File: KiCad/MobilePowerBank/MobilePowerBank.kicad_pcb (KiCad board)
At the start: 2 copper layers, 114 x 164 mm, 185 parts, among them J1 Power IN, J2 Power OUT 2, J3 Power OUT 1, J4 OLED I2C, J5 PDI, J6 OLED, J7 Power OUT 3, J8 Power OUT 4, J9 Power OUT 5, SW1 SW_DIP_x01, U1 INA169, U10 INA138, U11 LMZ14201H, U12 LMZ14201H, U13 INA138, U14 INA138, U15 ATXMEGA256A3U-AU, U2 LMZ14203H, U3 L78M12, U4 INA138, U5 UA78M33, U7 LMZ14203H, U8 LMZ14203H, U9 INA138

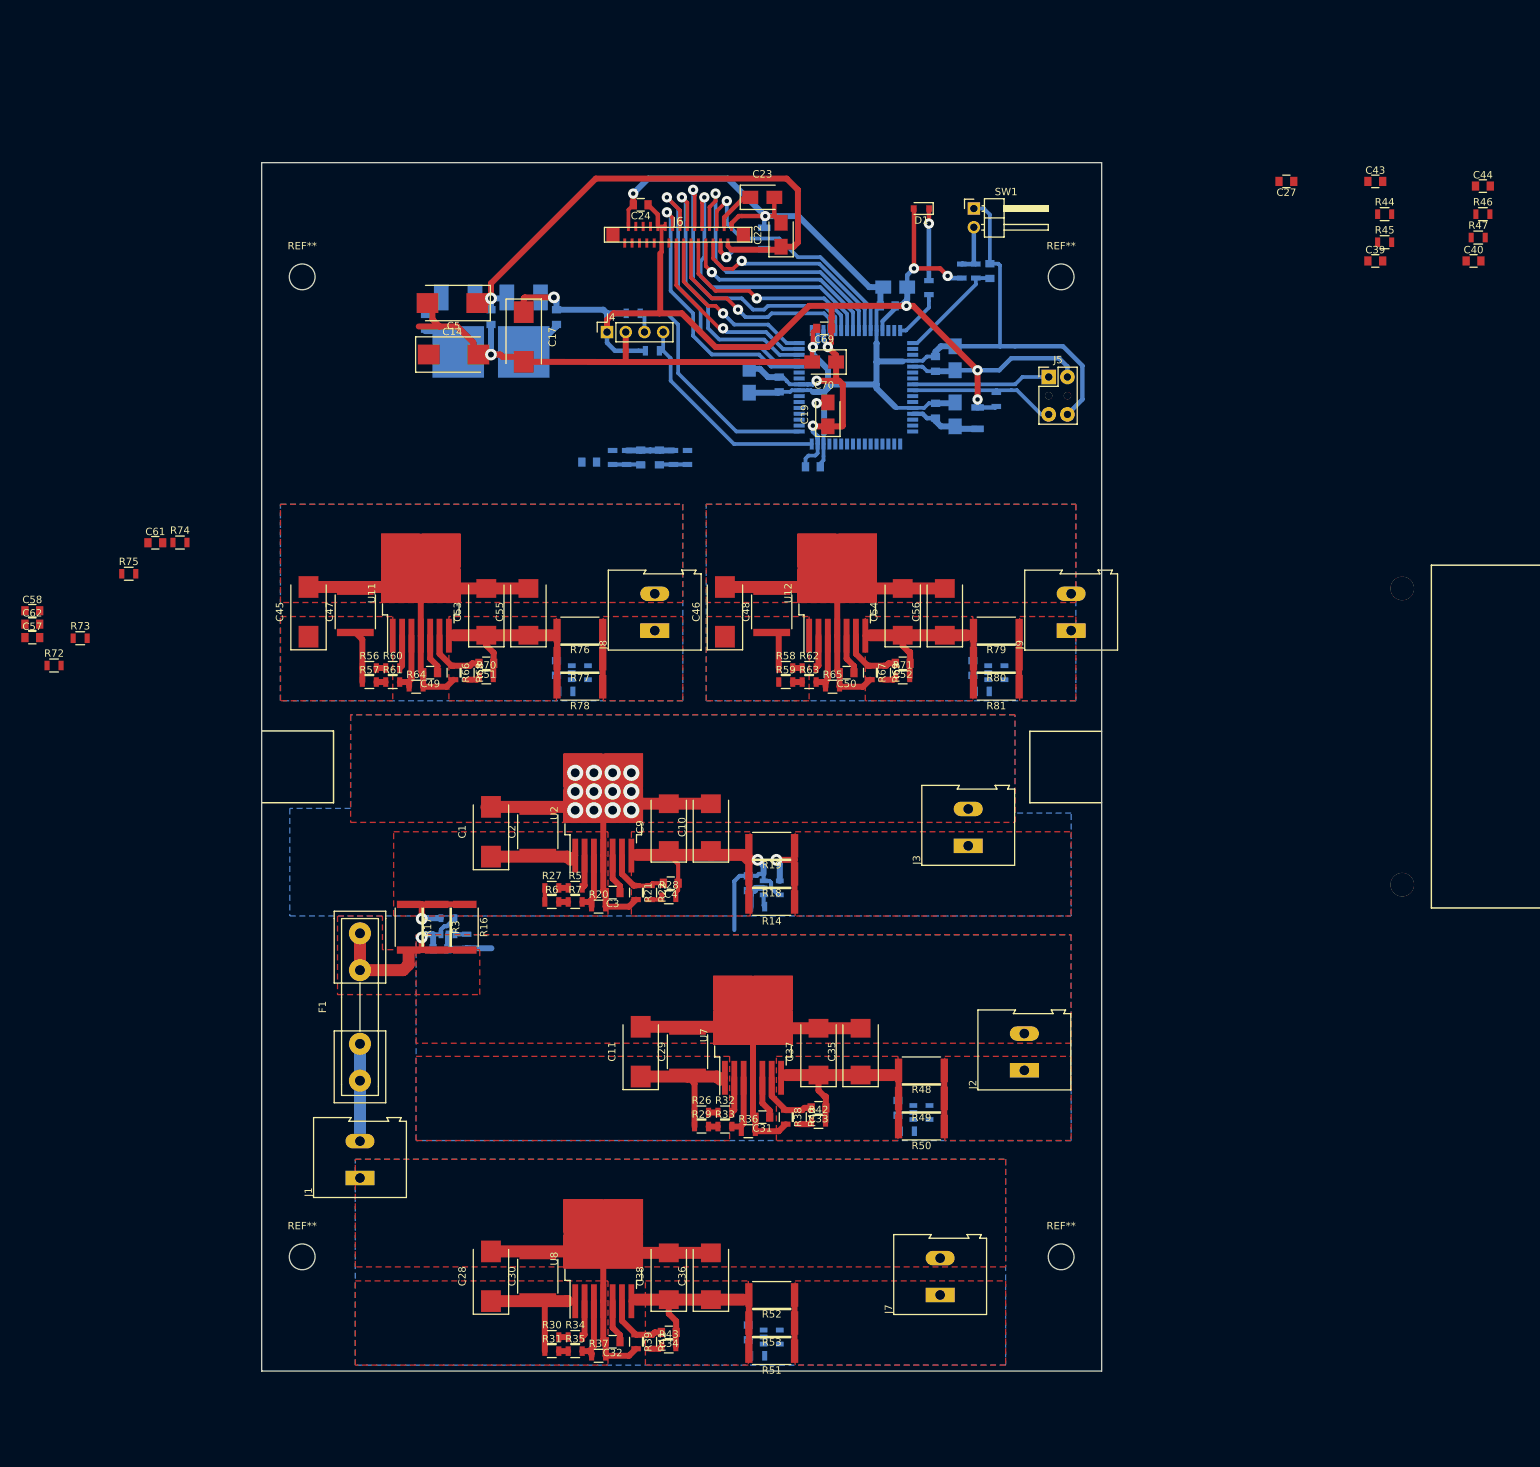
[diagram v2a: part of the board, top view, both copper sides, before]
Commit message: Bigger case
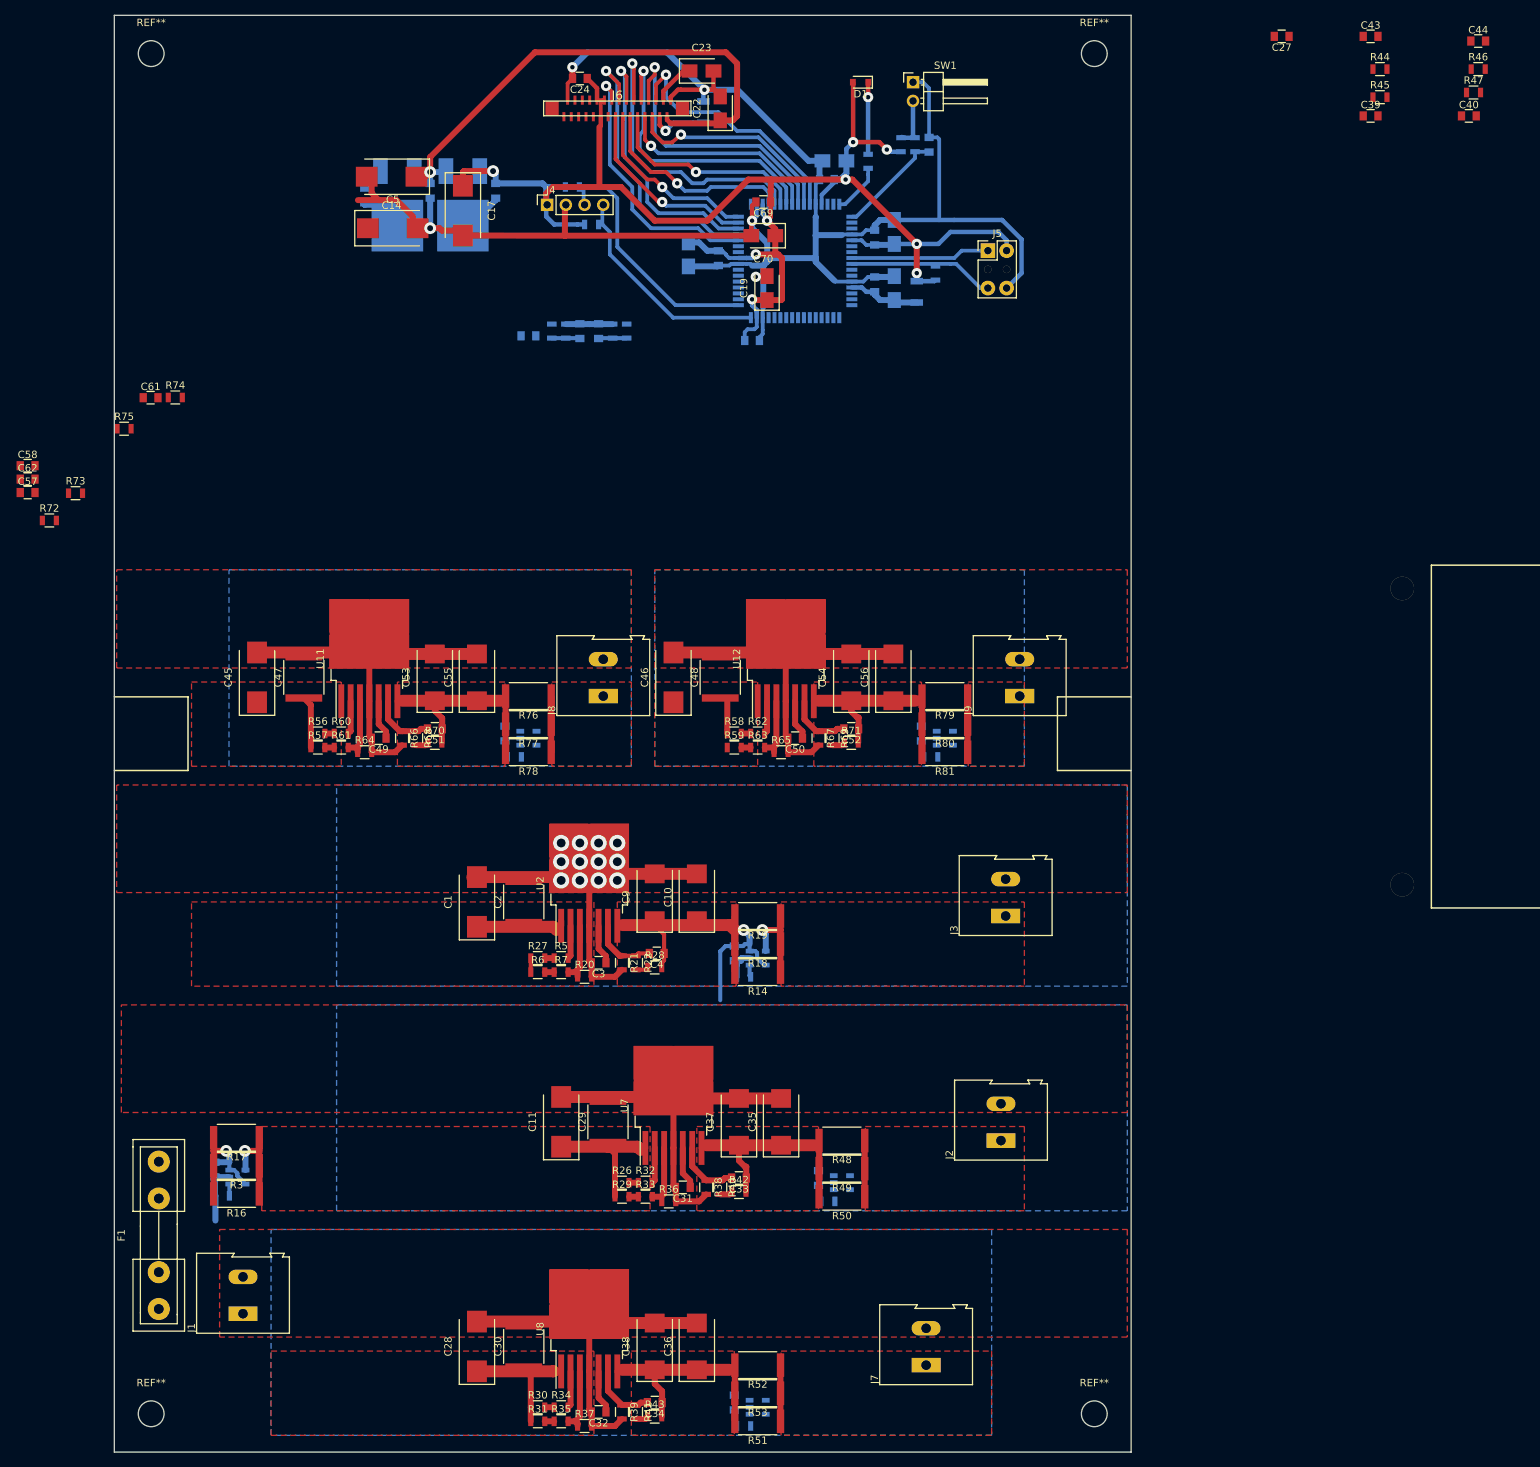
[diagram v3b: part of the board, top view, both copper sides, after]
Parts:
- moved R4 47.9 mm to (34.7, 180.2), turned to 180 degrees
- moved R16 47.6 mm to (36.6, 180.0), turned to 180 degrees
- moved U1 44.4 mm to (36.7, 177.7), turned to 0 degrees
- moved C7 42.8 mm to (33.7, 176.7), turned to 90 degrees
- moved R3 42.3 mm to (36.6, 176.1), turned to 180 degrees
- moved F1 41.3 mm to (26.0, 195.6)
- moved R17 36.9 mm to (36.6, 172.3), turned to 180 degrees
- moved REF** 36.6 mm to (25.0, 25.2)
- moved REF** 30.6 mm to (153.0, 25.2)
- moved REF** 29.6 mm to (25.0, 209.8)
- moved J1 24.3 mm to (37.5, 196.2)
- moved REF** 21.8 mm to (153.0, 209.8)
- moved R46 19.7 mm to (205.1, 27.3)
- moved C44 19.7 mm to (205.1, 23.5)
- moved C27 19.7 mm to (178.4, 22.9)
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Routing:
- net VDD: track 31.3 -> 17.5 mm
- net Net-(F1-Pad1): track 13.2 -> 0.00 mm
- removed copper zone on F.Cu, net VDD
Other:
- board size 114 x 164 mm -> 138 x 195 mm

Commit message: PCB major work
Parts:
- added C71: 47u, Capacitors_Tantalum_SMD:CP_Tantalum_Case-V_EIA-7343-20_Wave, F.Cu at (36.2, 78.7)
- added C72: 10u/35V/X7R, Capacitors_SMD:C_2220, F.Cu at (42.5, 78.7)
- added C73: 4u7, Capacitors_SMD:C_0805, F.Cu at (52.7, 87.0)
- added C74: 22n, Capacitors_SMD:C_0805, F.Cu at (60.3, 85.7)
- added C75: 47u/1-45mESR, Capacitors_Tantalum_SMD:CP_Tantalum_Case-D_EIA-7343-31_Reflow, F.Cu at (60.3, 78.7)
- added C76: 47u/1-45mESR, Capacitors_Tantalum_SMD:CP_Tantalum_Case-D_EIA-7343-31_Reflow, F.Cu at (66.0, 78.7)
- added C77: 100n, Capacitors_SMD:C_0805, B.Cu at (107.3, 75.6)
- added C78: 100n, Capacitors_SMD:C_0805, B.Cu at (81.9, 86.4)
- added C79: 1u, Capacitors_SMD:C_0805, B.Cu at (108.6, 71.8)
- added J10: Power OUT 6, Connectors_Terminal_Blocks:TerminalBlock_Altech_AK300-2_P5.00mm, F.Cu at (96.5, 81.3)
- added R84: 220k, Resistors_SMD:R_0805, F.Cu at (44.5, 86.4)
- added R85: 30k, Resistors_SMD:R_0805, F.Cu at (44.5, 88.3)
- added R86: 30k, Resistors_SMD:R_0805, F.Cu at (47.6, 86.4)
- added R87: 300k, Resistors_SMD:R_0805, F.Cu at (47.6, 88.3)
- added R88: 20k, Resistors_SMD:R_0805, F.Cu at (50.8, 88.9)
- added R89: 2k2, Resistors_SMD:R_0805, F.Cu at (55.9, 87.0)
- added R90: 15k4, Resistors_SMD:R_0805, F.Cu at (57.8, 87.0)
- added R91: 15k4, Resistors_SMD:R_0805, F.Cu at (60.3, 87.6)
- added R92: 90k, Resistors_SMD:R_0805, B.Cu at (107.3, 77.5)
- added R93: 10k, Resistors_SMD:R_0805, B.Cu at (107.3, 73.7)
- added R94: 0R1, Resistors_SMD:R_2512, F.Cu at (85.1, 85.0)
- added R95: 0R1, Resistors_SMD:R_2512, F.Cu at (85.1, 88.8)
- added R96: 0R1, Resistors_SMD:R_2512, F.Cu at (85.1, 81.2)
- added R97: 20k, Resistors_SMD:R_0805, B.Cu at (83.2, 89.5)
- added R98: 0, Resistors_SMD:R_0805, F.Cu at (104.1, 59.7)
- added U16: INA138, TO_SOT_Packages_SMD:SOT-23-5, B.Cu at (85.1, 87.0)
- added U6: LMZ14203H, TO_SOT_Packages_SMD:TO-263-7_TabPin4, F.Cu at (51.4, 76.2)
- added x1: jumper, JPJumpers:Jumper_30x1.5, F.Cu at (52.7, 192.4)
- added x2: jumper, JPJumpers:Jumper_30x1.5, F.Cu at (45.1, 161.9)
- added x3: jumper, JPJumpers:Jumper_30x1.5, F.Cu at (39.4, 134.0)
- added x4: jumper, JPJumpers:Jumper_30x1.5, F.Cu at (35.6, 103.5)
- added x5: jumper, JPJumpers:Jumper_45x1.5, F.Cu at (31.1, 65.4)
- C27, C39, C40, C43, C44, C57, C58, C61, C62, R44, R45, R46, R47, R72, R73, R74, R75: moved to B.Cu
- moved C62 113.8 mm to (121.9, 78.1), turned to 270 degrees
- moved C58 111.8 mm to (120.0, 79.4), turned to 90 degrees
- moved C57 103.9 mm to (111.8, 75.6)
- moved R72 101.2 mm to (111.8, 77.5), turned to 180 degrees
- moved R73 97.7 mm to (111.8, 73.7)
- moved R75 96.8 mm to (118.1, 79.4), turned to 90 degrees
- moved R74 94.7 mm to (122.6, 81.3), turned to 180 degrees
- moved C61 88.4 mm to (113.3, 71.8), turned to 180 degrees
- moved R47 85.6 mm to (125.7, 64.1), turned to 90 degrees
- moved C44 85.2 mm to (129.5, 62.9), turned to 270 degrees
- moved R46 84.3 mm to (130.2, 66.0), turned to 180 degrees
- moved C40 82.1 mm to (127.6, 64.1), turned to 90 degrees
- moved R45 78.4 mm to (123.2, 69.1), turned to 90 degrees
- moved C43 77.9 mm to (127.0, 67.9), turned to 270 degrees
- moved R44 77.7 mm to (127.6, 71.1), turned to 180 degrees
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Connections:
- C1 pad 1: POWER_IN -> POWER_IN_1
- C2 pad 1: POWER_IN -> POWER_IN_1
- C26 pad 2: GND -> GNDA
- C27 pad 2: GND -> GNDA
- C28 pad 1: POWER_IN -> POWER_IN_3
- C30 pad 1: POWER_IN -> POWER_IN_3
- C39 pad 2: GND -> GNDA
- C41 pad 1: GND -> GNDA
- C42 pad 1: GND -> GNDA
- C43 pad 2: GND -> GNDA
- C45 pad 1: POWER_IN -> POWER_IN_4
- C47 pad 1: POWER_IN -> POWER_IN_4
- C5 pad 1: POWER_IN -> Net-(C5-Pad1)
- C57 pad 2: GND -> GNDA
- C58 pad 2: GND -> GNDA
- C59 pad 1: GND -> GNDA
- C6 pad 1: POWER_IN -> Net-(C5-Pad1)
- C60 pad 1: GND -> GNDA
- C61 pad 2: GND -> GNDA
- C62 pad 2: GND -> GNDA
- C8 pad 1: GND -> GNDA
- R12 pad 1: Net-(C10-Pad1) -> POWER_1_OUT
- R13 pad 2: GND -> GNDA
- R15 pad 2: GND -> GNDA
- R27 pad 1: POWER_IN -> POWER_IN_1
- R30 pad 1: POWER_IN -> POWER_IN_3
- R31 pad 1: POWER_IN -> POWER_IN_3
- R44 pad 1: Net-(C33-Pad1) -> POWER_2_OUT
- R45 pad 2: GND -> GNDA
- R46 pad 1: Net-(C34-Pad1) -> POWER_3_OUT
- R47 pad 2: GND -> GNDA
- R54 pad 2: GND -> GNDA
- R55 pad 2: GND -> GNDA
- R56 pad 1: POWER_IN -> POWER_IN_4
- R57 pad 1: POWER_IN -> POWER_IN_4
- R6 pad 1: POWER_IN -> POWER_IN_1
- R72 pad 1: Net-(C51-Pad1) -> POWER_4_OUT
- R73 pad 2: GND -> GNDA
- R74 pad 1: Net-(C52-Pad1) -> POWER_5_OUT
- R75 pad 2: GND -> GNDA
- R82 pad 2: GND -> GNDA
- R83 pad 2: GND -> GNDA
- U10 pad 2: GND -> GNDA
- U11 pad 1: POWER_IN -> POWER_IN_4
- U13 pad 2: GND -> GNDA
- U14 pad 2: GND -> GNDA
- U15 pad 1: (no net) -> OUT_2_Current
- U15 pad 10: (no net) -> OUT_6_Voltage
- U15 pad 11: (no net) -> IN_Current
- U15 pad 12: (no net) -> IN_Voltage
- U15 pad 2: (no net) -> OUT_2_Voltage
- U15 pad 3: (no net) -> OUT_1_Current
- U15 pad 4: (no net) -> OUT_1_Voltage
- U15 pad 5: (no net) -> OUT_5_Current
- U15 pad 6: (no net) -> OUT_5_Voltage
- U15 pad 63: (no net) -> OUT_3_Current
- U15 pad 64: (no net) -> OUT_3_Voltage
- U15 pad 7: (no net) -> OUT_4_Current
- U15 pad 8: (no net) -> OUT_4_Voltage
- U15 pad 9: (no net) -> OUT_6_Current
- U2 pad 1: POWER_IN -> POWER_IN_1
- U3 pad 1: POWER_IN -> Net-(C5-Pad1)
- U4 pad 2: GND -> GNDA
- U8 pad 1: POWER_IN -> POWER_IN_3
- U9 pad 2: GND -> GNDA
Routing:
- net IN_Current: track 1.90 -> 232.2 mm
- net OUT_3_Current: track 0.00 -> 217.7 mm
- net VDD: track 17.5 -> 224.1 mm
- net OUT_2_Current: track 0.00 -> 179.0 mm
- net POWER_3_OUT: track 7.62 -> 183.7 mm, vias 0 -> 1
- net OUT_1_Current: track 1.65 -> 158.0 mm
- net POWER_2_OUT: track 7.62 -> 136.2 mm, vias 0 -> 1
- net GNDA: track 309.8 -> 436.9 mm, vias 12 -> 59
- net POWER_1_OUT: track 13.1 -> 104.5 mm
- net OUT_4_Current: track 0.00 -> 85.4 mm
- net OUT_5_Current: track 0.00 -> 58.9 mm
- net POWER_4_OUT: track 7.62 -> 59.7 mm, vias 0 -> 1
- net Net-(C74-Pad1): track 0.00 -> 50.9 mm, vias 0 -> 1
- net OUT_6_Current: track 0.00 -> 50.4 mm
- net POWER_IN_1: track 0.00 -> 46.6 mm
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- added copper zone on B.Cu, net GND
- added copper zone on F.Cu, net Net-(C74-Pad1)
- added copper zone on B.Cu, net Net-(F1-Pad1)
- added copper zone on F.Cu, net Net-(F1-Pad1)
- added copper zone on F.Cu, net POWER_6_OUT
- added copper zone on F.Cu, net POWER_IN_1
- added copper zone on F.Cu, net POWER_IN_3
- added copper zone on F.Cu, net POWER_IN_4
- added copper zone on F.Cu, net POWER_IN_6
- added copper zone on F.Cu, net VDD

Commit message: PCB finish, BOM check
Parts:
- added x6: jumper, JPJumpers:Jumper_30x1.5, F.Cu at (44.7, 146.7)
- added x7: jumper, JPJumpers:Jumper_30x1.5, F.Cu at (52.3, 177.2)
- added x8: jumper, JPJumpers:Jumper_30x1.5, F.Cu at (26.9, 82.8)
- added x9: jumper, JPJumpers:Jumper_30x1.5, F.Cu at (31.5, 115.8)
- moved R47 136.3 mm to (135.9, 200.0)
- moved R46 135.9 mm to (134.0, 201.9), turned to 90 degrees
- moved R2 129.5 mm to (28.6, 172.7), turned to 0 degrees
- moved R1 128.2 mm to (26.0, 172.1)
- moved R45 102.4 mm to (146.1, 168.9)
- moved R44 101.1 mm to (144.1, 170.8), turned to 90 degrees
- moved R13 69.8 mm to (146.7, 139.1)
- moved R12 67.7 mm to (144.8, 141.0), turned to 90 degrees
- moved R98 63.9 mm to (40.6, 52.8)
- moved R72 38.7 mm to (90.2, 109.6), turned to 90 degrees
- moved R73 37.0 mm to (89.5, 103.3), turned to 180 degrees
- moved R75 12.5 mm to (129.5, 84.5), turned to 180 degrees
- moved R74 8.98 mm to (131.4, 82.5)
- moved C62 7.41 mm to (118.1, 71.8), turned to 180 degrees
- moved R92 7.15 mm to (100.3, 79.0), turned to 90 degrees
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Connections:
- C26 pad 2: GNDA -> GND
- C27 pad 2: GNDA -> GND
- C39 pad 2: GNDA -> GND
- C43 pad 2: GNDA -> GND
- C46 pad 1: POWER_IN -> POWER_IN_4
- C48 pad 1: POWER_IN -> POWER_IN_4
- C57 pad 2: GNDA -> GND
- C58 pad 2: GNDA -> GND
- C61 pad 2: GNDA -> GND
- C62 pad 2: GNDA -> GND
- C7 pad 1: GND -> GNDA
- C77 pad 2: GNDA -> GND
- C79 pad 2: GNDA -> GND
- R2 pad 2: GND -> GNDA
- R4 pad 2: GND -> GNDA
- R58 pad 1: POWER_IN -> POWER_IN_4
- R59 pad 1: POWER_IN -> POWER_IN_4
- U1 pad 2: GND -> GNDA
- U12 pad 1: POWER_IN -> POWER_IN_4
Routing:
- net IN_Voltage: track 14.5 -> 220.5 mm
- net VDD: track 224.1 -> 18.3 mm
- net OUT_3_Voltage: track 12.7 -> 181.2 mm
- net POWER_3_OUT: track 183.7 -> 16.3 mm
- net OUT_2_Voltage: track 16.0 -> 139.4 mm
- net POWER_2_OUT: track 136.2 -> 16.6 mm
- net OUT_1_Voltage: track 20.8 -> 109.0 mm
- net POWER_1_OUT: track 104.5 -> 16.3 mm
- net GND: track 306.8 -> 391.0 mm, vias 5 -> 12
- net POWER_IN_4: track 24.1 -> 89.5 mm
- net POWER_4_OUT: track 59.7 -> 16.3 mm
- net OUT_4_Voltage: track 17.3 -> 57.0 mm
- net POWER_IN_1: track 46.6 -> 14.4 mm
- net GNDA: track 436.9 -> 424.9 mm, vias 59 -> 54
- net OUT_5_Voltage: track 25.4 -> 34.7 mm
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- added copper zone on F.Cu, net GND

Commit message: Cap changed
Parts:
- C1, C11, C28, C45, C46, C5, C71: value 47u -> 47u/35V
- C13: value 47u -> 100n
- C14: value 100u -> 47u/16V
- C17: value 47u -> 47u/6.3V
- C19, C21, C64, C66, C68, C70: value 10u -> 10u/6.3V
- C22, C23: value 10u -> 10u/16V
- R14, R16, R17, R18, R19, R3, R48, R49, R50, R51, R52, R53, R76, R77, R78, R79, R80, R81, R94, R95, R96: value 0R1 -> 0R033
- R22: value 15k4 -> 47k
- R27: value 220k -> 300k
- R28: value 15k4 -> 4k7
- R29, R31, R57, R59, R85: value 30k -> 47k
- R5: value 30k -> 100k
- R6: value 30k -> 68k
- U1: value INA169 -> INA139
- U10, U13, U14, U16, U4, U9: value INA138 -> INA139
- moved REF** 150.5 mm to (90.8, 78.7)
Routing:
- net POWER_IN_3: track 35.0 -> 32.5 mm
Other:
- board text added: "JP"
- board text added: "MobilePowerSupply v1 JP, 2018.10.15"
